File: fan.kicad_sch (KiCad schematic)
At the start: 18 parts, among them J5 Conn_01x04, J6 Conn_01x04, U10 TMP1075, U11 TMP1075, U12 EMC2302

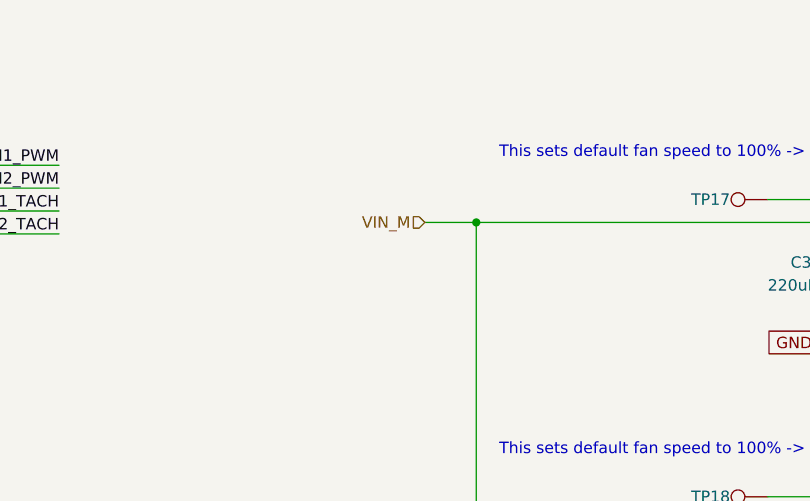
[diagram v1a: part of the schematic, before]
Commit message: remove INA219 power monitor
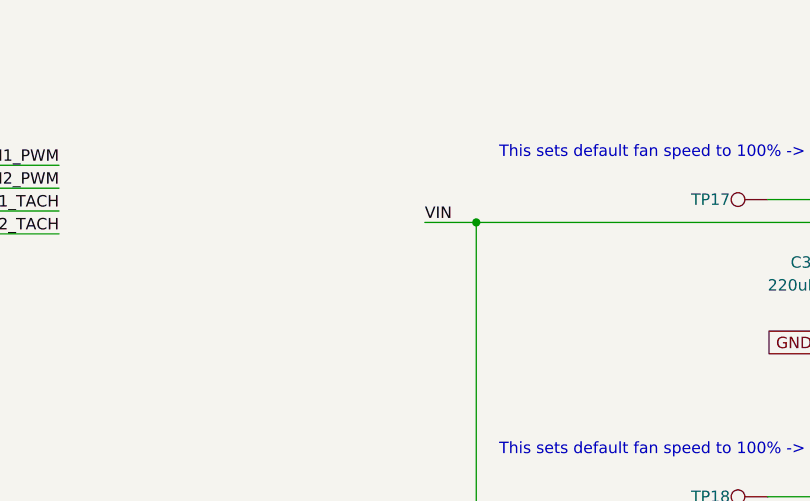
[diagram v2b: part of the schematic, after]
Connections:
- net VIN_M renamed VIN
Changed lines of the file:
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@@
+    (effects (font (size 1.27 1.27)) (justify left bottom))
+  )
+  (label "VIN" (at 157.48 53.34 0) (fields_autoplaced)
     (effects (font (size 1.27 1.27)) (justify left bottom))
   )
@@
     )
   )
-  (hierarchical_label "VIN_M" (shape input) (at 157.48 53.34 180) (fields_autoplaced)
-    (effects (font (size 1.27 1.27)) (justify right))
-  )
   (hierarchical_label "SCL" (shape input) (at 71.755 52.07 180) (fields_autoplaced)

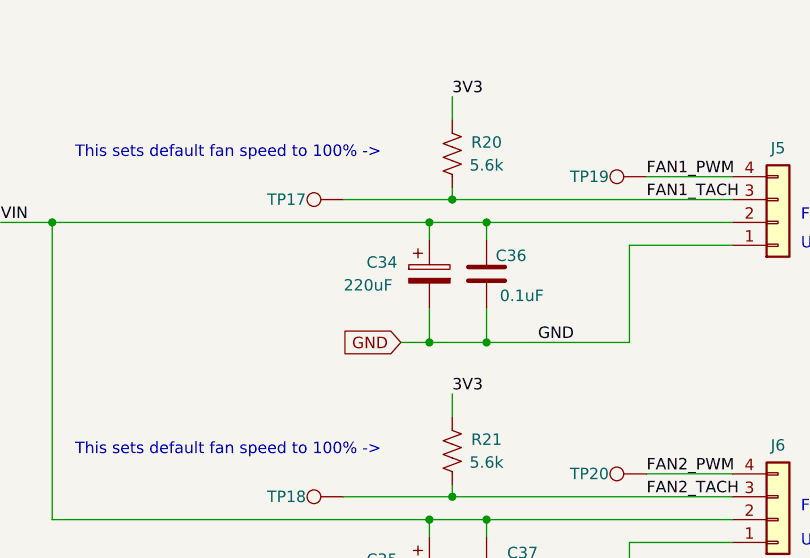
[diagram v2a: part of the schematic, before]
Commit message: 5V pullups on fan tachs
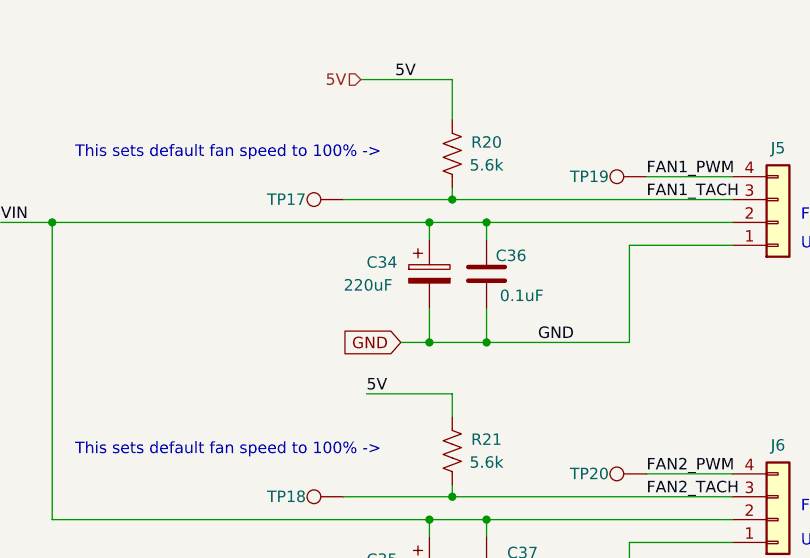
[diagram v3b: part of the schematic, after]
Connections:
- net 3V3: no longer R20.2, R21.2
- new net 5V: R20.2, R21.2
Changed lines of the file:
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@@
+    (stroke (width 0) (type default))
+  )
+  (wire (pts (xy 198.12 72.39) (xy 207.645 72.39))
     (stroke (width 0) (type default))
   )
@@
     (stroke (width 0) (type default))
   )
-  (wire (pts (xy 207.645 39.37) (xy 207.645 41.91))
-    (stroke (width 0) (type default))
-  )
   (wire (pts (xy 74.93 125.73) (xy 74.93 133.35))
     (stroke (width 0) (type default))
@@
     (stroke (width 0) (type default))
   )
+  (wire (pts (xy 105.41 120.65) (xy 109.855 120.65))
+    (stroke (width 0) (type default))
+  )
+  (wire (pts (xy 74.93 106.045) (xy 74.93 102.235))
+    (stroke (width 0) (type default))
+  )
+  (wire (pts (xy 99.695 137.795) (xy 105.41 137.795))
+    (stroke (width 0) (type default))
+  )
+  (wire (pts (xy 195.58 83.82) (xy 207.645 83.82))
+    (stroke (width 0) (type default))
+  )
+  (wire (pts (xy 78.74 133.35) (xy 74.93 133.35))
+    (stroke (width 0) (type default))
+  )
+  (wire (pts (xy 163.195 53.34) (xy 205.105 53.34))
+    (stroke (width 0) (type default))
+  )
   (wire (pts (xy 207.645 72.39) (xy 207.645 74.93))
     (stroke (width 0) (type default))
   )
-  (wire (pts (xy 105.41 120.65) (xy 109.855 120.65))
-    (stroke (width 0) (type default))
-  )
-  (wire (pts (xy 74.93 106.045) (xy 74.93 102.235))
-    (stroke (width 0) (type default))
-  )
-  (wire (pts (xy 99.695 137.795) (xy 105.41 137.795))
-    (stroke (width 0) (type default))
-  )
-  (wire (pts (xy 195.58 83.82) (xy 207.645 83.82))
-    (stroke (width 0) (type default))
-  )
-  (wire (pts (xy 78.74 133.35) (xy 74.93 133.35))
-    (stroke (width 0) (type default))
-  )
-  (wire (pts (xy 163.195 53.34) (xy 205.105 53.34))
-    (stroke (width 0) (type default))
-  )
   (wire (pts (xy 211.455 86.36) (xy 211.455 88.265))
     (stroke (width 0) (type default))
@@
     (stroke (width 0) (type default))
   )
+  (wire (pts (xy 197.485 37.465) (xy 207.645 37.465))
+    (stroke (width 0) (type default))
+  )
   (wire (pts (xy 227.33 55.88) (xy 238.76 55.88))
     (stroke (width 0) (type default))
@@
   )
   (wire (pts (xy 67.945 102.235) (xy 74.93 102.235))
+    (stroke (width 0) (type default))
+  )
+  (wire (pts (xy 207.645 37.465) (xy 207.645 41.91))
     (stroke (width 0) (type default))
   )
@@
     (effects (font (size 1.27 1.27)) (justify left bottom))
   )
-  (label "3V3" (at 207.645 39.37 0) (fields_autoplaced)
+  (label "5V" (at 201.295 37.465 0) (fields_autoplaced)
     (effects (font (size 1.27 1.27)) (justify left bottom))
   )
@@
     (effects (font (size 1.27 1.27)) (justify left bottom))
   )
-  (label "3V3" (at 207.645 72.39 0) (fields_autoplaced)
+  (label "5V" (at 198.12 72.39 0) (fields_autoplaced)
     (effects (font (size 1.27 1.27)) (justify left bottom))
   )
@@
     )
   )
+  (hierarchical_label "5V" (shape input) (at 197.485 37.465 180) (fields_autoplaced)
+    (effects (font (size 1.27 1.27)) (justify right))
+  )
   (hierarchical_label "SCL" (shape input) (at 71.755 52.07 180) (fields_autoplaced)

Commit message: parts placement for new regulator
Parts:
- C34, C35: HEIGHT (none) -> 7.7mm
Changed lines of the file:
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@@
       (effects (font (size 1.27 1.27)) hide)
     )
-    (property "Datasheet" "~" (at 205.105 92.075 0)
+    (property "Datasheet" "https://www.we-online.com/components/products/datasheet/865080345012.pdf" (at 205.105 92.075 0)
       (effects (font (size 1.27 1.27)) hide)
     )
@@
     )
     (property "PARTNO" "865080345012" (at 205.105 92.075 0)
+      (effects (font (size 1.27 1.27)) hide)
+    )
+    (property "HEIGHT" "7.7mm" (at 205.105 92.075 0)
       (effects (font (size 1.27 1.27)) hide)
     )
@@
       (effects (font (size 1.27 1.27)) hide)
     )
-    (property "Datasheet" "~" (at 205.105 59.055 0)
+    (property "Datasheet" "https://www.we-online.com/components/products/datasheet/865080345012.pdf" (at 205.105 59.055 0)
       (effects (font (size 1.27 1.27)) hide)
     )
@@
       (effects (font (size 1.27 1.27)) hide)
     )
+    (property "HEIGHT" "7.7mm" (at 205.105 59.055 0)
+      (effects (font (size 1.27 1.27)) hide)
+    )

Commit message: more routing
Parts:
- added R114, R115: 10K, Resistor_SMD:R_0402_1005Metric, symbol Device:R_US
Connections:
- net 3V3: now also R20.2, R21.2
- net 5V: now also R114.2, R115.2; no longer R20.2, R21.2
- net FAN1_PWM: now also R114.1
- net FAN2_PWM: now also R115.1
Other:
- moved on the sheet: C35, C37, J6, R21, TP18, TP19, TP20

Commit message: re-annotate all components
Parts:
- renumbered C31 to C38, C32 to C39, C33 to C40, C34 to C41, C35 to C42, C36 to C43, C37 to C44, J5 to J8, J6 to J9, R20 to R26, R21 to R27, R115 to R28, R114 to R29, TP17 to TP30, TP18 to TP31, TP20 to TP32, TP19 to TP33, U10 to U7, U11 to U8, U12 to U9

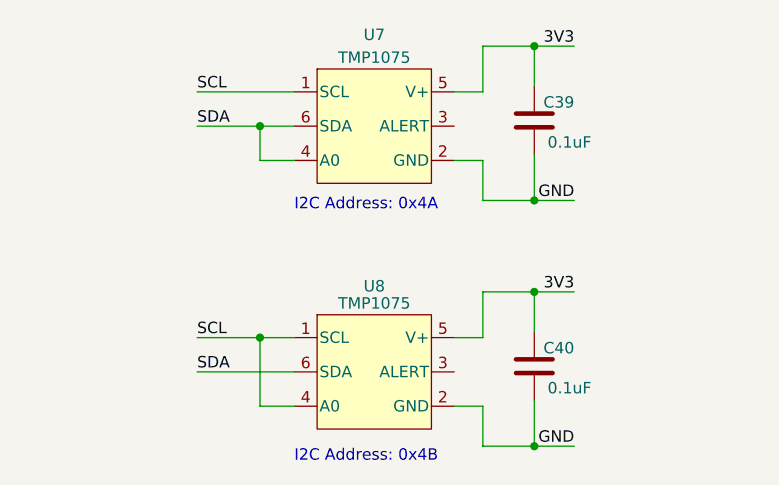
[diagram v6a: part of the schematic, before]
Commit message: increase size of copper planes, generate final BOM
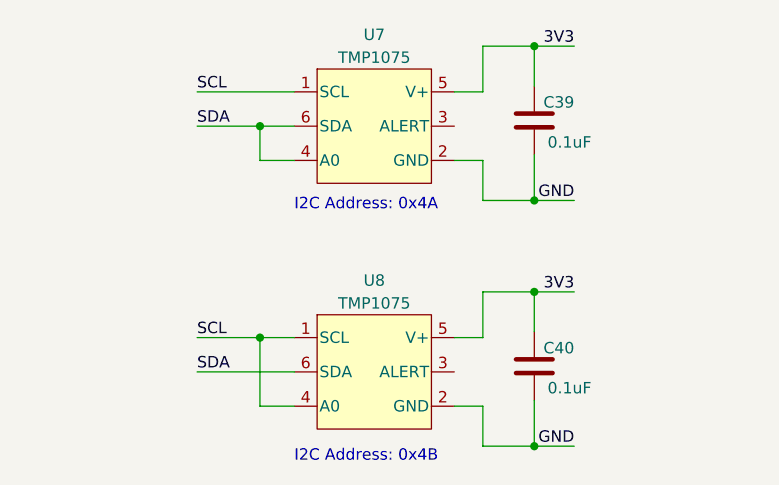
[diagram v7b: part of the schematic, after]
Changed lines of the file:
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@@
+    )
+  )
+  (symbol (lib_name "TMP1075NDRLR_1") (lib_id "bitaxe:TMP1075NDRLR") (at 87.63 128.27 0) (unit 1)
+    (in_bom yes) (on_board yes) (dnp no)
+    (property "Reference" "U8" (at 87.63 119.38 0)
+      (effects (font (size 1.27 1.27)))
+    )
+    (property "Value" "TMP1075" (at 87.63 121.92 0)
+      (effects (font (size 1.27 1.27)))
+    )
+    (property "Footprint" "bitaxe:SOT5X3-6_DRL_TEX" (at 114.3 140.97 0)
+      (effects (font (size 1.27 1.27) italic) hide)
+    )
+    (property "Datasheet" "https://www.ti.com/lit/ds/symlink/tmp1075.pdf" (at 111.76 114.3 0)
+      (effects (font (size 1.27 1.27) italic) hide)
+    )
+    (property "DK" "296-TMP1075NDRLRCT-ND" (at 87.63 128.27 0)
+      (effects (font (size 1.27 1.27)) hide)
+    )
+    (property "PARTNO" "TMP1075NDRLR" (at 87.63 128.27 0)
+      (effects (font (size 1.27 1.27)) hide)
+    )
+    (pin "1")
+    (pin "2")
+    (pin "3")
+    (pin "4")
+    (pin "5")
+    (pin "6")
+    (instances
+      (project "bitaxeHex"
+        (path "/e63e39d7-6ac0-4ffd-8aa3-1841a4541b55/8e8832ea-6bf1-49d2-b3a5-32a207f555d2"
+          (reference "U8") (unit 1)
+        )
+      )
     )
   )
@@
         )
       )
-    )
-  )
-  (symbol (lib_id "bitaxe:TMP1075NDRLR") (at 87.63 128.27 0) (unit 1)
-    (in_bom yes) (on_board yes) (dnp no)
-    (property "Reference" "U8" (at 87.63 120.015 0)
-      (effects (font (size 1.27 1.27)))
-    )
-    (property "Value" "TMP1075" (at 87.63 121.92 0)
-      (effects (font (size 1.27 1.27)))
-    )
-    (property "Footprint" "bitaxe:SOT5X3-6_DRL_TEX" (at 114.3 140.97 0)
-      (effects (font (size 1.27 1.27) italic) hide)
-    )
-    (property "Datasheet" "https://www.ti.com/lit/ds/symlink/tmp1075.pdf" (at 111.76 114.3 0)
-      (effects (font (size 1.27 1.27) italic) hide)
-    )
-    (property "PARTNO" "TMP1075NDRLR" (at 87.63 128.27 0)
-      (effects (font (size 1.27 1.27)) hide)
-    )
-    (property "DK" "296-TMP1075NDRLRCT-ND" (at 87.63 128.27 0)
-      (effects (font (size 1.27 1.27)) hide)
-    )
-    (pin "1")
-    (pin "2")
-    (pin "3")
-    (pin "4")
-    (pin "5")
-    (pin "6")
-    (instances
-      (project "bitaxeHex"
-        (path "/e63e39d7-6ac0-4ffd-8aa3-1841a4541b55/8e8832ea-6bf1-49d2-b3a5-32a207f555d2"
-          (reference "U8") (unit 1)
-        )
-      )

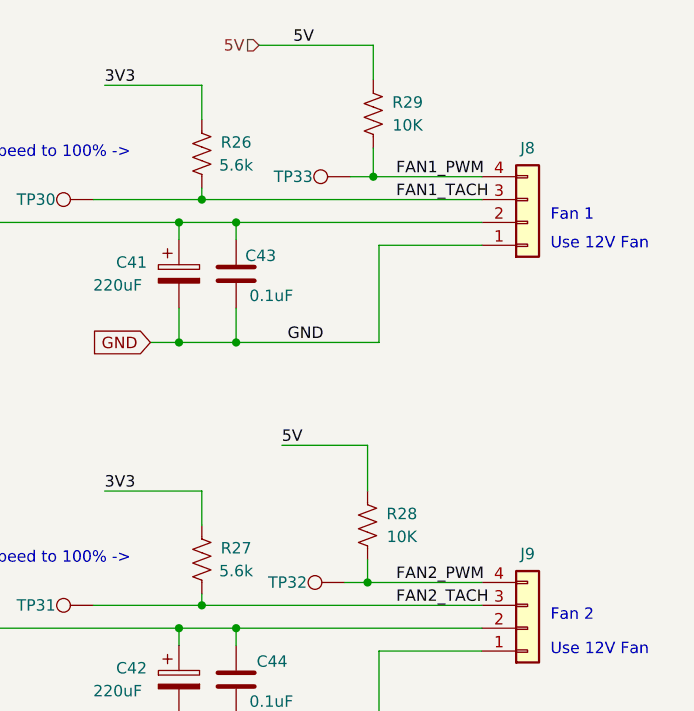
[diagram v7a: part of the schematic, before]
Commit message: BOM adjustments to R28, R29, config resistors
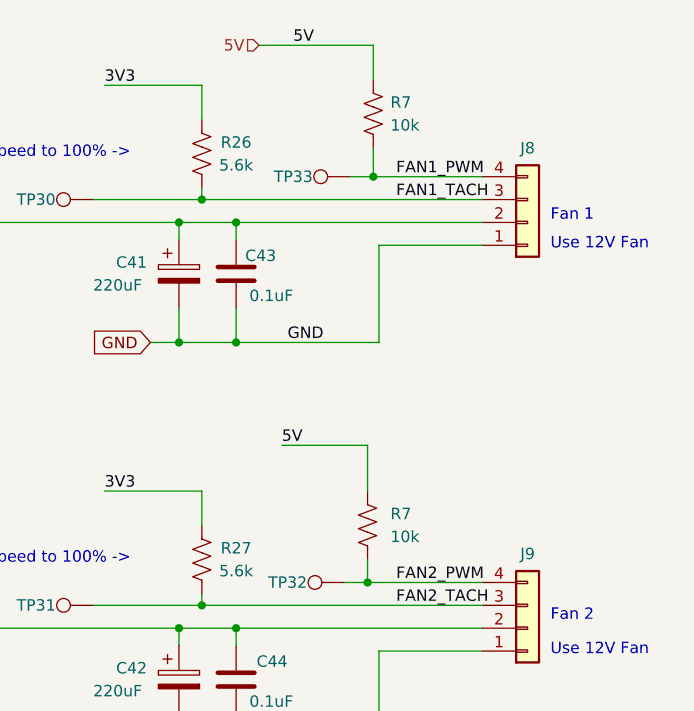
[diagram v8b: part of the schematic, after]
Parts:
- removed R28, R29: 10K, Resistor_SMD:R_0402_1005Metric, symbol Device:R_US
- added R7 (x2): 10k, Resistor_SMD:R_0402_1005Metric, symbol Device:R_US
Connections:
- net 5V: now also R7.2, R7.2
- net FAN1_PWM: now also R7.1
- net FAN2_PWM: now also R7.1
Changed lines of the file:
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@@
+    )
+  )
+  (symbol (lib_id "Device:R_US") (at 226.695 41.275 180) (unit 1)
+    (in_bom yes) (on_board yes) (dnp no) (fields_autoplaced)
+    (property "Reference" "R7" (at 228.6 40.005 0)
+      (effects (font (size 1.27 1.27)) (justify right))
+    )
+    (property "Value" "10k" (at 228.6 42.545 0)
+      (effects (font (size 1.27 1.27)) (justify right))
+    )
+    (property "Footprint" "Resistor_SMD:R_0402_1005Metric" (at 225.679 41.021 90)
+      (effects (font (size 1.27 1.27)) hide)
+    )
+    (property "Datasheet" "~" (at 226.695 41.275 0)
+      (effects (font (size 1.27 1.27)) hide)
+    )
+    (property "DK" "311-10KJRCT-ND" (at 226.695 41.275 0)
+      (effects (font (size 1.27 1.27)) hide)
+    )
+    (property "PARTNO" "RC0402JR-0710KL" (at 226.695 41.275 0)
+      (effects (font (size 1.27 1.27)) hide)
+    )
+    (pin "1")
+    (pin "2")
+    (instances
+      (project "esp32"
+        (path "/dcd2fc1c-da48-40a9-b97c-5712d9530f4f"
+          (reference "R7") (unit 1)
+        )
+      )
+      (project "bitaxeHex"
+        (path "/e63e39d7-6ac0-4ffd-8aa3-1841a4541b55/ca857324-2ec8-447e-bd58-90d0c2e6b6d7"
+          (reference "R22") (unit 1)
+        )
+        (path "/e63e39d7-6ac0-4ffd-8aa3-1841a4541b55/8e8832ea-6bf1-49d2-b3a5-32a207f555d2"
+          (reference "R29") (unit 1)
+        )
+      )
     )
   )
@@
     )
   )
+  (symbol (lib_id "Device:R_US") (at 226.06 86.995 180) (unit 1)
+    (in_bom yes) (on_board yes) (dnp no) (fields_autoplaced)
+    (property "Reference" "R7" (at 228.6 85.725 0)
+      (effects (font (size 1.27 1.27)) (justify right))
+    )
+    (property "Value" "10k" (at 228.6 88.265 0)
+      (effects (font (size 1.27 1.27)) (justify right))
+    )
+    (property "Footprint" "Resistor_SMD:R_0402_1005Metric" (at 225.044 86.741 90)
+      (effects (font (size 1.27 1.27)) hide)
+    )
+    (property "Datasheet" "~" (at 226.06 86.995 0)
+      (effects (font (size 1.27 1.27)) hide)
+    )
+    (property "DK" "311-10KJRCT-ND" (at 226.06 86.995 0)
+      (effects (font (size 1.27 1.27)) hide)
+    )
+    (property "PARTNO" "RC0402JR-0710KL" (at 226.06 86.995 0)
+      (effects (font (size 1.27 1.27)) hide)
+    )
+    (pin "1")
+    (pin "2")
+    (instances
+      (project "esp32"
+        (path "/dcd2fc1c-da48-40a9-b97c-5712d9530f4f"
+          (reference "R7") (unit 1)
+        )
+      )
+      (project "bitaxeHex"
+        (path "/e63e39d7-6ac0-4ffd-8aa3-1841a4541b55/ca857324-2ec8-447e-bd58-90d0c2e6b6d7"
+          (reference "R22") (unit 1)
+        )
+        (path "/e63e39d7-6ac0-4ffd-8aa3-1841a4541b55/8e8832ea-6bf1-49d2-b3a5-32a207f555d2"
+          (reference "R28") (unit 1)
+        )
+      )
+    )
+  )
   (symbol (lib_id "Connector_Generic:Conn_01x04") (at 243.84 53.34 0) (mirror x) (unit 1)
     (in_bom yes) (on_board yes) (dnp no)
@@
         (path "/e63e39d7-6ac0-4ffd-8aa3-1841a4541b55/8e8832ea-6bf1-49d2-b3a5-32a207f555d2"
           (reference "J8") (unit 1)
-        )
-      )
-    )
-  )
-  (symbol (lib_id "Device:R_US") (at 226.06 86.995 180) (unit 1)
-    (in_bom yes) (on_board yes) (dnp no)
-    (property "Reference" "R28" (at 229.87 85.725 0)
-      (effects (font (size 1.27 1.27)))
-    )
-    (property "Value" "10K" (at 229.87 88.265 0)
-      (effects (font (size 1.27 1.27)))
-    )
-    (property "Footprint" "Resistor_SMD:R_0402_1005Metric" (at 225.044 86.741 90)
-      (effects (font (size 1.27 1.27)) hide)
-    )
-    (property "Datasheet" "~" (at 226.06 86.995 0)
-      (effects (font (size 1.27 1.27)) hide)
-    )
-    (property "DK" "13-RC0402FR-135K6LCT-ND" (at 226.06 86.995 0)
-      (effects (font (size 1.27 1.27)) hide)
-    )
-    (property "PARTNO" "RC0402FR-135K6L" (at 226.06 86.995 0)
-      (effects (font (size 1.27 1.27)) hide)
-    )
-    (pin "1")
-    (pin "2")
-    (instances
-      (project "bitaxeHex"
-        (path "/e63e39d7-6ac0-4ffd-8aa3-1841a4541b55/8e8832ea-6bf1-49d2-b3a5-32a207f555d2"
-          (reference "R28") (unit 1)
         )
       )
@@
         )
       )
-    )
-  )
-  (symbol (lib_id "Device:R_US") (at 226.695 41.275 180) (unit 1)
-    (in_bom yes) (on_board yes) (dnp no)
-    (property "Reference" "R29" (at 230.505 40.005 0)
-      (effects (font (size 1.27 1.27)))
-    )
-    (property "Value" "10K" (at 230.505 42.545 0)
-      (effects (font (size 1.27 1.27)))
-    )
-    (property "Footprint" "Resistor_SMD:R_0402_1005Metric" (at 225.679 41.021 90)
-      (effects (font (size 1.27 1.27)) hide)
-    )
-    (property "Datasheet" "~" (at 226.695 41.275 0)
-      (effects (font (size 1.27 1.27)) hide)
-    )
-    (property "DK" "13-RC0402FR-135K6LCT-ND" (at 226.695 41.275 0)
-      (effects (font (size 1.27 1.27)) hide)
-    )
-    (property "PARTNO" "RC0402FR-135K6L" (at 226.695 41.275 0)
-      (effects (font (size 1.27 1.27)) hide)
-    )
-    (pin "1")
-    (pin "2")
-    (instances
-      (project "bitaxeHex"
-        (path "/e63e39d7-6ac0-4ffd-8aa3-1841a4541b55/8e8832ea-6bf1-49d2-b3a5-32a207f555d2"
-          (reference "R29") (unit 1)
-        )
-      )
